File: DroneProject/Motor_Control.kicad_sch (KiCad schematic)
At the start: 1 part, among them U81 STM32G431KBT6

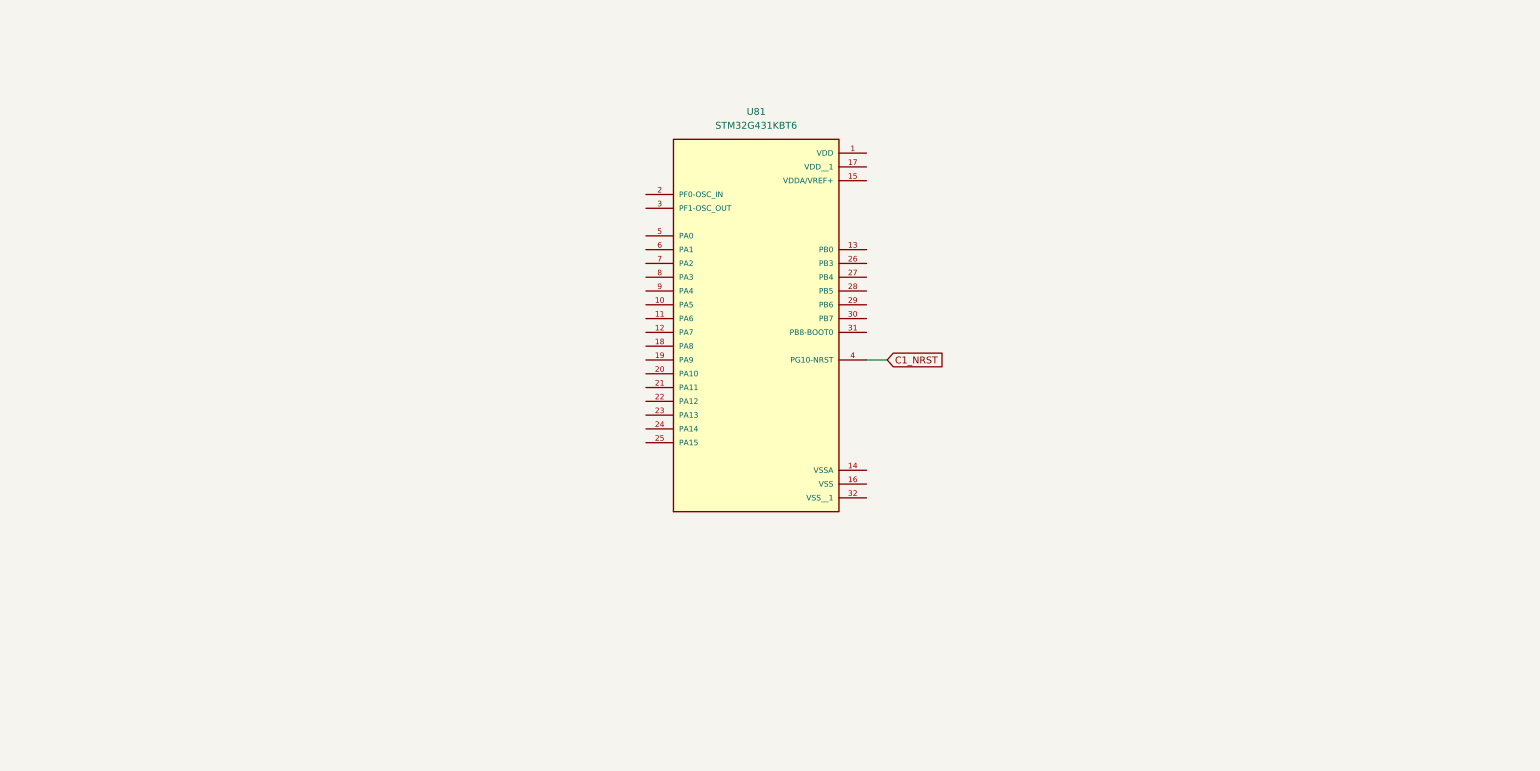
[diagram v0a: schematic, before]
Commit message: Changed motor controller to higher pin count MCU.  Defined all the pins for 3x PWM control over 4 motors.  Renamed a couple of global IO signals to indicate MCU origin (C0 vs C1)
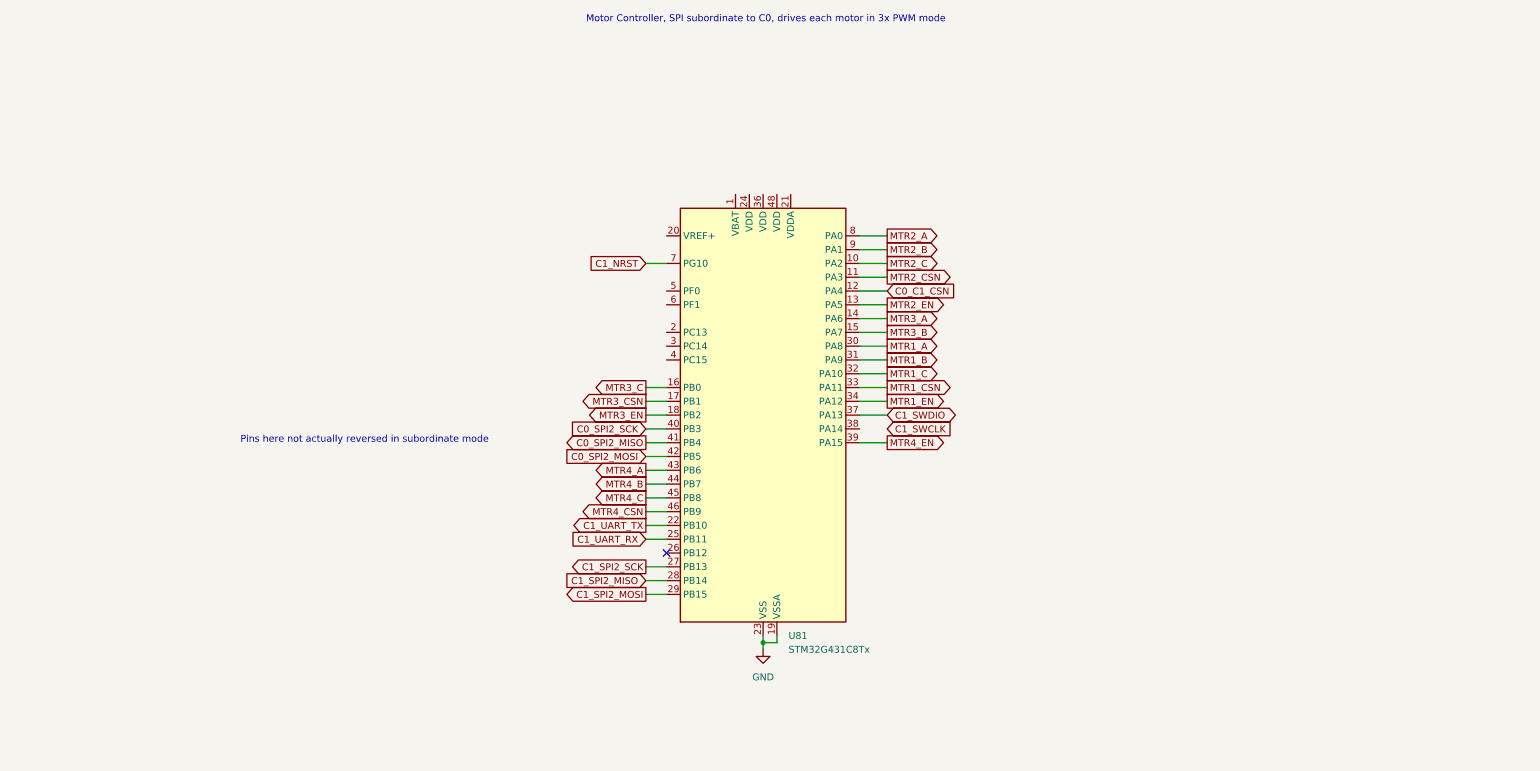
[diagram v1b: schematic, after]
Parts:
- removed U81: STM32G431KBT6, Library:QFP80P900X900X160-32N, symbol Global:STM32G431KBT6
- added U81: STM32G431C8Tx, Package_QFP:LQFP-48_7x7mm_P0.5mm, symbol MCU_ST_STM32G4:STM32G431C8Tx
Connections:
- net C1_NRST: now also U81.7 (PG10)
- new net C0_C1_CSN: U81.12 (PA4)
- new net C0_SPI2_MISO: U81.41 (PB4)
- new net C0_SPI2_MOSI: U81.42 (PB5)
- new net C0_SPI2_SCK: U81.40 (PB3)
- new net C1_SPI2_MISO: U81.28 (PB14)
- new net C1_SPI2_MOSI: U81.29 (PB15)
- new net C1_SPI2_SCK: U81.27 (PB13)
- new net C1_SWDIO: U81.37 (PA13)
- new net C1_UART_RX: U81.25 (PB11)
- new net C1_UART_TX: U81.22 (PB10)
- new net GND: U81.19 (VSSA), U81.23 (VSS), U81.35 (VSS), U81.47 (VSS)
- new net MTR1_A: U81.30 (PA8)
- new net MTR1_B: U81.31 (PA9)
- new net MTR1_C: U81.32 (PA10)
- new net MTR1_CSN: U81.33 (PA11)
- new net MTR1_EN: U81.34 (PA12)
- new net MTR2_A: U81.8 (PA0)
- new net MTR2_B: U81.9 (PA1)
- new net MTR2_C: U81.10 (PA2)
- new net MTR2_CSN: U81.11 (PA3)
- new net MTR2_EN: U81.13 (PA5)
- new net MTR3_A: U81.14 (PA6)
- new net MTR3_B: U81.15 (PA7)
- new net MTR3_C: U81.16 (PB0)
- new net MTR3_CSN: U81.17 (PB1)
- new net MTR3_EN: U81.18 (PB2)
- new net MTR4_A: U81.43 (PB6)
- new net MTR4_B: U81.44 (PB7)
- new net MTR4_C: U81.45 (PB8)
- new net MTR4_CSN: U81.46 (PB9)
- new net MTR4_EN: U81.39 (PA15)
- no-connect marks 0 -> 1
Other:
- note added: "Motor Controller, SPI subordinate to C0, drives each motor in 3x PWM mode"
- note added: "Pins here not actually reversed in subordinate mode"

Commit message: Finished motor and C1 designs, still need to rename components on MTR2, 3, and 4 pages
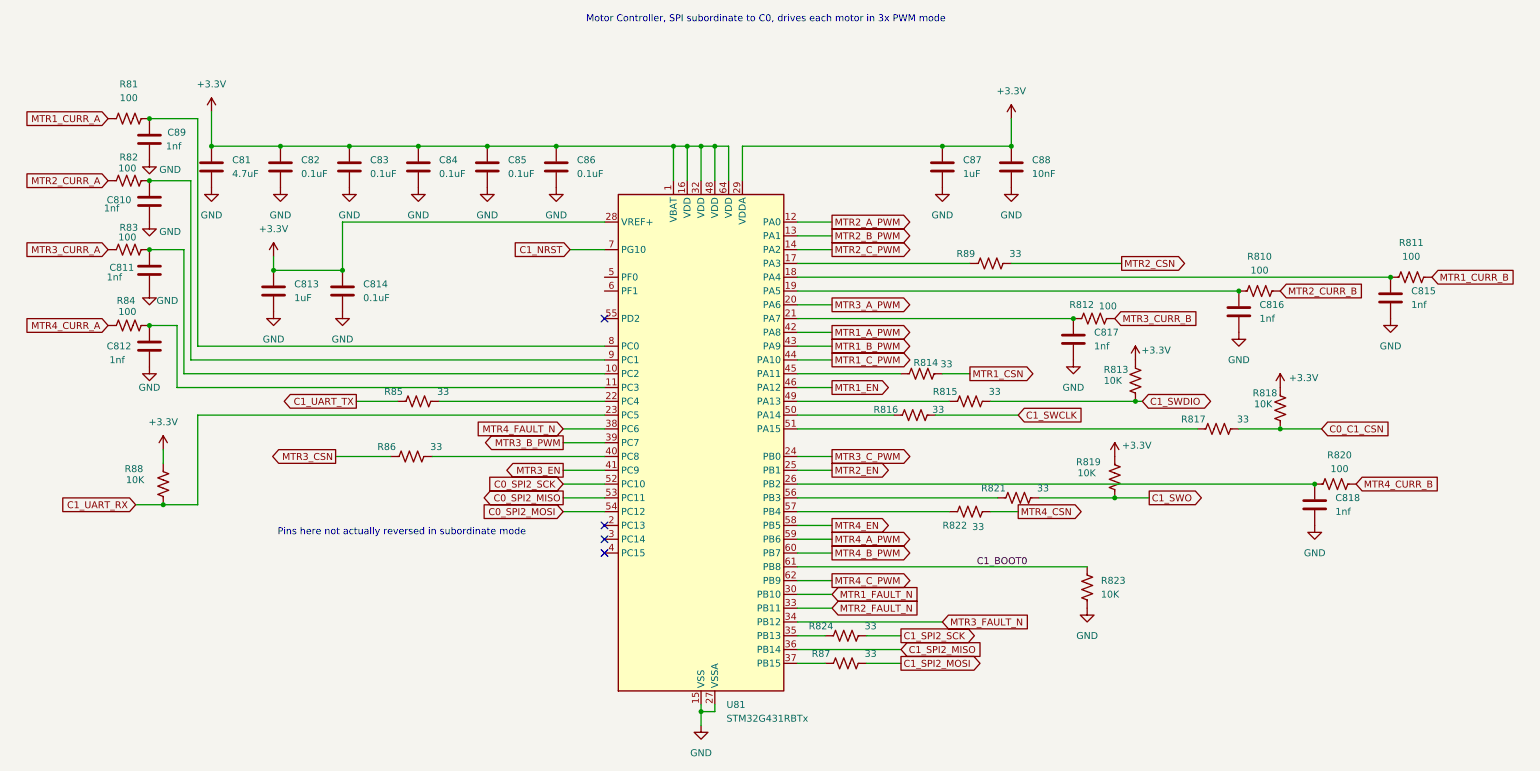
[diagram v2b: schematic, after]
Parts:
- removed U81: STM32G431C8Tx, Package_QFP:LQFP-48_7x7mm_P0.5mm, symbol MCU_ST_STM32G4:STM32G431C8Tx
- added C81: 4.7uF, Capacitor_SMD:C_0805_2012Metric, symbol Device:C
- added C810, C811, C812, C815, C816, C817, C818, C89: 1nf, Capacitor_SMD:C_0402_1005Metric, symbol Device:C
- added C813, C87: 1uF, Capacitor_SMD:C_0402_1005Metric, symbol Device:C
- added C814, C82, C83, C84, C85, C86: 0.1uF, Capacitor_SMD:C_0402_1005Metric, symbol Device:C
- added C88: 10nF, Capacitor_SMD:C_0402_1005Metric, symbol Device:C
- added R81, R810, R811, R812, R82, R820, R83, R84: 100, Resistor_SMD:R_0402_1005Metric, symbol Device:R_US
- added R813, R818, R819, R823, R88: 10K, Resistor_SMD:R_0402_1005Metric, symbol Device:R_US
- added R814, R815, R816, R817, R821, R822, R824, R85, R86, R87, R89: 33, Resistor_SMD:R_0402_1005Metric, symbol Device:R_US
- added U81: STM32G431RBTx, Package_QFP:LQFP-64_10x10mm_P0.5mm, symbol MCU_ST_STM32G4:STM32G431RBTx
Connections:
- net C0_C1_CSN: now also R817.2, R818.1
- net C0_SPI2_MISO: now also U81.53 (PC11)
- net C0_SPI2_MOSI: now also U81.54 (PC12)
- net C0_SPI2_SCK: now also U81.52 (PC10)
- net C1_NRST: now also U81.7 (PG10)
- net C1_SPI2_MISO: now also U81.36 (PB14)
- net C1_SPI2_MOSI: now also R87.2
- net C1_SPI2_SCK: now also R824.2
- net C1_SWCLK: now also R816.2
- net C1_SWDIO: now also R813.1, R815.2
- net C1_UART_RX: now also R88.1, U81.23 (PC5)
- net C1_UART_TX: now also R85.1
- net GND: now also C81.2, C810.2, C811.2, C812.2, C813.2, C814.2, C815.2, C816.2, C817.2, C818.2, C82.2, C83.2, C84.2, C85.2, C86.2, C87.2, C88.2, C89.2, R823.1, U81.15 (VSS), U81.27 (VSSA), U81.31 (VSS), U81.47 (VSS), U81.63 (VSS)
- net MTR1_CSN: now also R814.2
- net MTR1_EN: now also U81.46 (PA12)
- net MTR2_CSN: now also R89.2
- net MTR2_EN: now also U81.25 (PB1)
- net MTR3_CSN: now also R86.1
- net MTR3_EN: now also U81.41 (PC9)
- net MTR4_CSN: now also R822.2
- net MTR4_EN: now also U81.58 (PB5)
- new net: C818.1, R820.1, U81.26 (PB2)
- new net: R86.2, U81.40 (PC8)
- new net: C815.1, R811.1, U81.18 (PA4)
- new net: C811.1, R83.2, U81.10 (PC2)
- new net: R815.1, U81.49 (PA13)
- new net: C810.1, R82.2, U81.9 (PC1)
- new net: C817.1, R812.1, U81.21 (PA7)
- new net: C816.1, R810.1, U81.19 (PA5)
- new net: R821.1, U81.56 (PB3)
- new net: R822.1, U81.57 (PB4)
- new net: C812.1, R84.2, U81.11 (PC3)
- new net: R89.1, U81.17 (PA3)
- new net: R85.2, U81.22 (PC4)
- new net: R824.1, U81.35 (PB13)
- new net: R87.1, U81.37 (PB15)
- new net: R814.1, U81.45 (PA11)
- new net: R816.1, U81.50 (PA14)
- new net: R817.1, U81.51 (PA15)
- new net: C89.1, R81.2, U81.8 (PC0)
- new net +3.3V: C81.1, C813.1, C814.1, C82.1, C83.1, C84.1, C85.1, C86.1, C87.1, C88.1, R813.2, R818.2, R819.2, R88.2, U81.1 (VBAT), U81.16 (VDD), U81.28 (VREF+), U81.29 (VDDA), U81.32 (VDD), U81.48 (VDD), U81.64 (VDD)
- new net C1_BOOT0: R823.2, U81.61 (PB8)
- new net C1_SWO: R819.1, R821.2
- new net MTR1_A_PWM: U81.42 (PA8)
- new net MTR1_B_PWM: U81.43 (PA9)
- new net MTR1_CURR_A: R81.1
- new net MTR1_CURR_B: R811.2
- new net MTR1_C_PWM: U81.44 (PA10)
- new net MTR1_FAULT_N: U81.30 (PB10)
- new net MTR2_A_PWM: U81.12 (PA0)
- new net MTR2_B_PWM: U81.13 (PA1)
- new net MTR2_CURR_A: R82.1
- new net MTR2_CURR_B: R810.2
- new net MTR2_C_PWM: U81.14 (PA2)
- new net MTR2_FAULT_N: U81.33 (PB11)
- new net MTR3_A_PWM: U81.20 (PA6)
- new net MTR3_B_PWM: U81.39 (PC7)
- new net MTR3_CURR_A: R83.1
- new net MTR3_CURR_B: R812.2
- new net MTR3_C_PWM: U81.24 (PB0)
- new net MTR3_FAULT_N: U81.34 (PB12)
- new net MTR4_A_PWM: U81.59 (PB6)
- new net MTR4_B_PWM: U81.60 (PB7)
- new net MTR4_CURR_A: R84.1
- new net MTR4_CURR_B: R820.2
- new net MTR4_C_PWM: U81.62 (PB9)
- new net MTR4_FAULT_N: U81.38 (PC6)
- no-connect marks 1 -> 4

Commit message: Finished most of routing for motor controls, however likely going to revert back and make separate ESC boards for motor control as I think that would honestly be more efficient from both a cost and debug complexity standpoint.
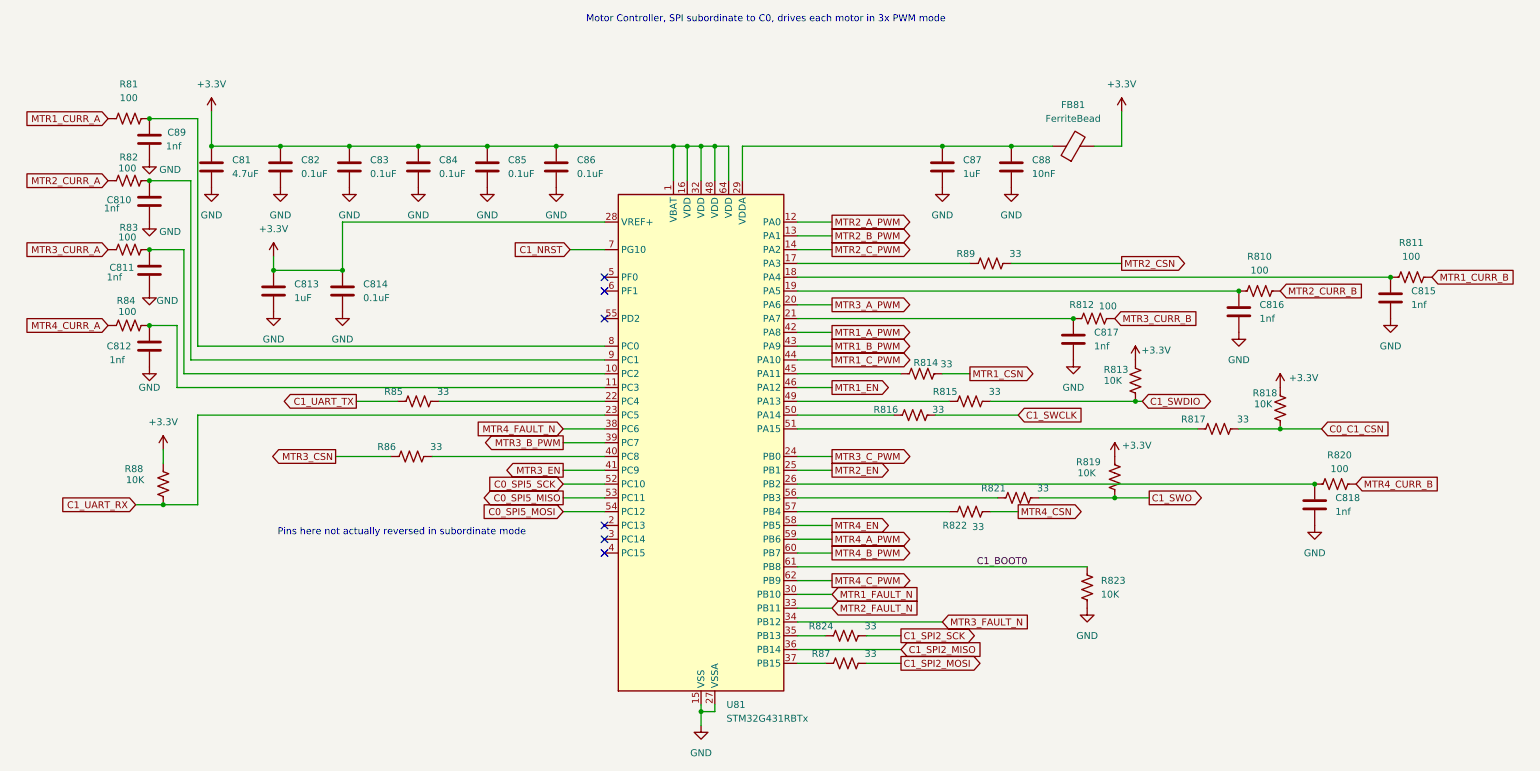
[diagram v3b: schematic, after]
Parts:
- added FB81: FerriteBead, Inductor_SMD:L_0805_2012Metric, symbol Device:FerriteBead
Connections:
- net +3.3V: now also FB81.2; no longer C87.1, C88.1, U81.29 (VDDA)
- net C0_SPI2_MISO renamed C0_SPI5_MISO
- net C0_SPI2_MOSI renamed C0_SPI5_MOSI
- net C0_SPI2_SCK renamed C0_SPI5_SCK
- new net: C87.1, C88.1, FB81.1, U81.29 (VDDA)
- no-connect marks 4 -> 6
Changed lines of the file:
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@@
 	)
 	(junction
+		(at 191.77 48.26)
+		(diameter 0)
+		(color 0 0 0 0)
+	)
+	(junction
 		(at 33.02 54.61)
 		(diameter 0)
@@
 	)
 	(junction
-		(at 191.77 48.26)
-		(diameter 0)
-		(color 0 0 0 0)
-	)
-	(junction
 		(at 44.45 48.26)
 		(diameter 0)
@@
 	)
 	(no_connect
+		(at 116.84 74.93)
+	)
+	(no_connect
 		(at 116.84 118.11)
 	)
@@
 		(at 116.84 123.19)
 	)
+	(no_connect
+		(at 116.84 72.39)
+	)
 	(wire
 		(pts
@@
 	(wire
 		(pts
-			(xy 191.77 43.18) (xy 191.77 48.26)
+			(xy 212.09 41.91) (xy 212.09 48.26)
 		)
 		(stroke
@@
 	(wire
 		(pts
+			(xy 191.77 48.26) (xy 199.39 48.26)
+		)
+		(stroke
+			(width 0)
+			(type default)
+		)
+	)
+	(wire
+		(pts
 			(xy 142.24 54.61) (xy 142.24 48.26)
 		)
@@
 		)
 	)
+	(wire
+		(pts
+			(xy 207.01 48.26) (xy 212.09 48.26)
+		)
+		(stroke
+			(width 0)
+			(type default)
+		)
+	)
 	(label "C1_BOOT0"
 		(at 185.42 125.73 0)
@@
 		)
 	)
-	(global_label "C0_SPI2_MISO"
+	(global_label "C0_SPI5_MISO"
 		(shape output)
 		(at 109.22 113.03 180)
@@
 		)
 	)
-	(global_label "C0_SPI2_SCK"
+	(global_label "C0_SPI5_SCK"
 		(shape input)
 		(at 109.22 110.49 180)
@@
 		)
 	)
-	(global_label "C0_SPI2_MOSI"
+	(global_label "C0_SPI5_MOSI"
 		(shape input)
 		(at 109.22 115.57 180)
@@
 	)
 	(symbol
+		(lib_id "Device:FerriteBead")
+		(at 203.2 48.26 90)
+		(unit 1)
+		(exclude_from_sim no)
+		(in_bom yes)
+		(on_board yes)
+		(dnp no)
+		(fields_autoplaced yes)
+		(property "Reference" "FB81"
+			(at 203.1492 40.64 90)
+			(effects
+				(font
+					(size 1.27 1.27)
+				)
+			)
+		)
+		(property "Value" "FerriteBead"
+			(at 203.1492 43.18 90)
+			(effects
+				(font
+					(size 1.27 1.27)
+				)
+			)
+		)
+		(property "Footprint" "Inductor_SMD:L_0805_2012Metric"
+			(at 203.2 50.038 90)
+			(effects
+				(font
+					(size 1.27 1.27)
+				)
+				(hide yes)
+			)
+		)
+		(property "Datasheet" "~"
+			(at 203.2 48.26 0)
+			(effects
+				(font
+					(size 1.27 1.27)
+				)
+				(hide yes)
+			)
+		)
+		(property "Description" "Ferrite bead"
+			(at 203.2 48.26 0)
+			(effects
+				(font
+					(size 1.27 1.27)
+				)
+				(hide yes)
+			)
+		)
+		(pin "1"
+		)
+		(pin "2"
+		)
+		(instances
+			(project "DroneProject"
+				(path "/feb4ca7b-5376-4689-a73b-f56020a5aa30/b6a115f3-035a-43b2-b989-cf27d7328b3b"
+					(reference "FB81")
+					(unit 1)
+				)
+			)
+		)
+	)
+	(symbol
 		(lib_id "power:GND")
 		(at 44.45 55.88 0)
@@
 	(symbol
 		(lib_id "power:+3.3V")
-		(at 191.77 43.18 0)
+		(at 212.09 41.91 0)
 		(unit 1)
 		(exclude_from_sim no)
@@
 		(fields_autoplaced yes)
 		(property "Reference" "#PWR0137"
-			(at 191.77 46.99 0)
+			(at 212.09 45.72 0)
 			(effects
 				(font
@@
 		)
 		(property "Value" "+3.3V"
-			(at 191.77 38.1 0)
+			(at 212.09 36.83 0)
 			(effects
 				(font
@@
 		)
 		(property "Footprint" ""
-			(at 191.77 43.18 0)
+			(at 212.09 41.91 0)
 			(effects
 				(font
@@
 		)
 		(property "Datasheet" ""
-			(at 191.77 43.18 0)
+			(at 212.09 41.91 0)
 			(effects
 				(font
@@
 		)
 		(property "Description" "Power symbol creates a global label with name \"+3.3V\""
-			(at 191.77 43.18 0)
+			(at 212.09 41.91 0)
 			(effects
 				(font
